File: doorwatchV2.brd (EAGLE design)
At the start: 91.4 x 77.5 mm, 43 parts, among them IC1 LM2576S-5.0, IC2 MAX3232CPE, K1 FINDER-43.61, Q1 IRLZ44Z, T1 BC847, T2 BC847, T3 BC847, T4 BC847, X1 MKDSN1,5/2-5,08, X2 D-SUB9-H2M09RA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

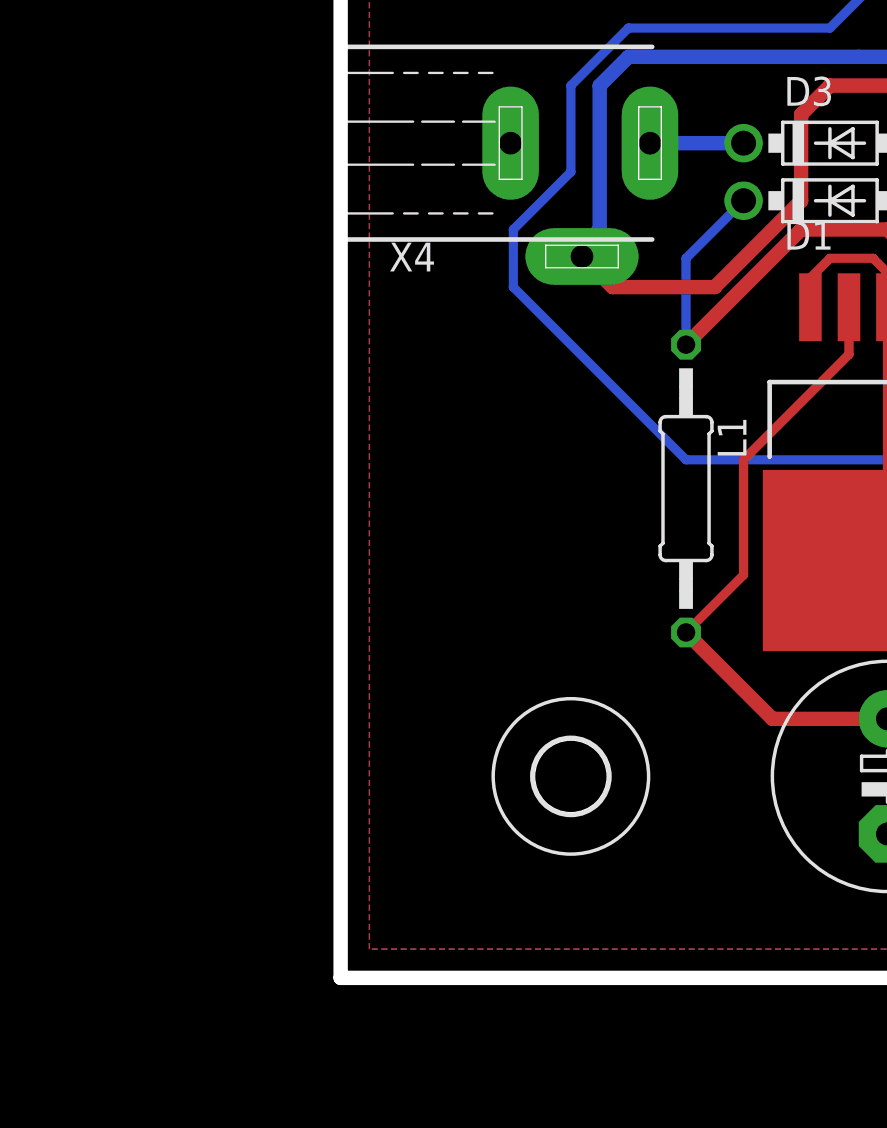
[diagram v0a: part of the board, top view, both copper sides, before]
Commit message: fixed two bugs: 1) wrong polarity of power-jack 2) missing pull-down resistor on output of LTV826 opto-coupler, in front of MOSFET IRLZ44Z
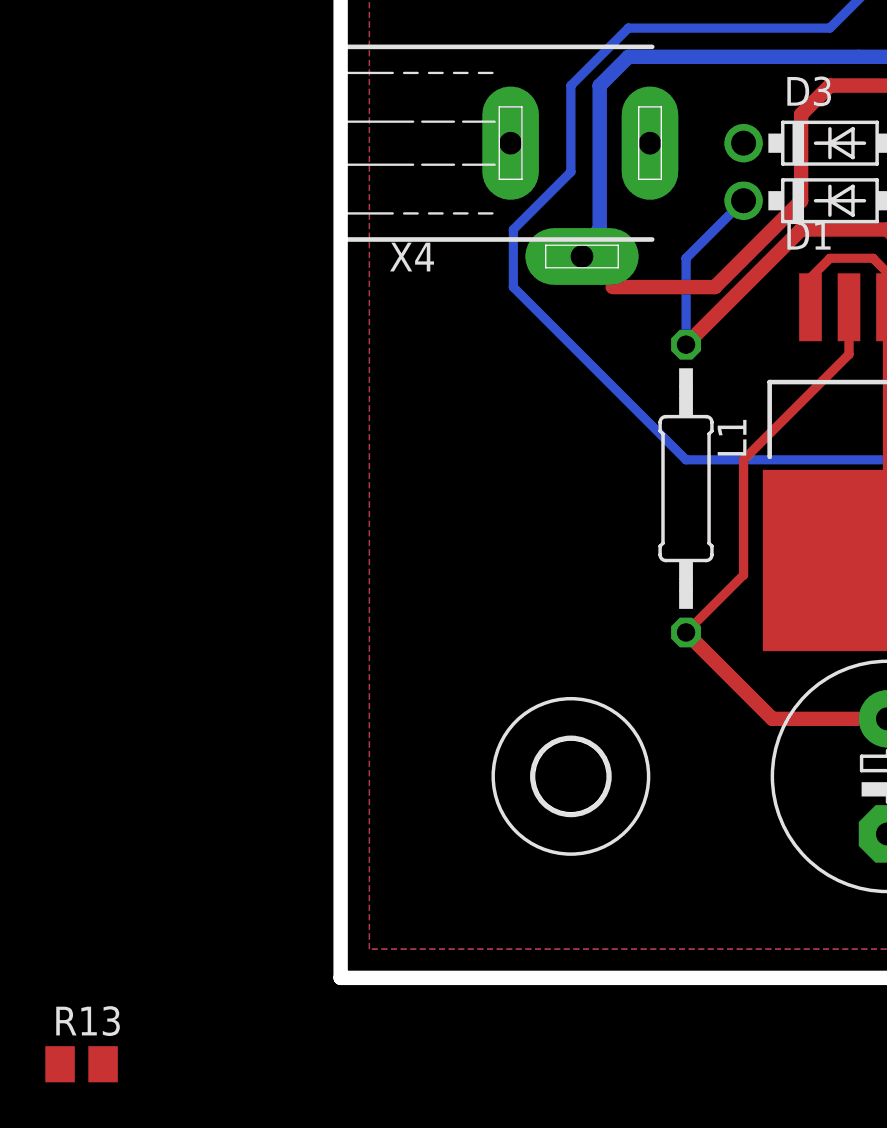
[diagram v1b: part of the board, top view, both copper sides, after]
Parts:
- added R13: 1k, rcl:M0805
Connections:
- net +12V: now also X4.1; no longer X4.3
- net GND: now also R13.1
- net N$15: now also X4.2, X4.3; no longer X4.1
- net N$16: now also R13.2
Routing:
- net N$15: track 4.13 -> 0.00 mm
- net +12V: track 131.0 -> 129.1 mm
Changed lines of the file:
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@@
 <element name="H2" library="holes" package="3,2" value="MOUNT-HOLE3.2" x="55.88" y="93.98"/>
 <element name="H3" library="holes" package="3,2" value="MOUNT-HOLE3.2" x="81.28" y="33.02"/>
+<element name="R13" library="rcl" package="M0805" value="1k" x="-12.7" y="20.32"/>
 </elements>
 <signals>
@@
 <wire x1="20.32" y1="55.88" x2="22.225" y2="55.88" width="0.4064" layer="1"/>
 <wire x1="22.225" y1="55.88" x2="22.86" y2="55.245" width="0.4064" layer="1"/>
+<contactref element="R13" pad="1"/>
+<wire x1="77.47" y1="82.23" x2="82.525" y2="82.5289" width="0" layer="19" extent="16-16"/>
+<wire x1="69.85" y1="55.56" x2="77.47" y2="82.23" width="0" layer="19" extent="16-16"/>
+<wire x1="69.85" y1="46.04" x2="69.85" y2="55.56" width="0" layer="19" extent="16-16"/>
+<wire x1="67.31" y1="31.97" x2="69.85" y2="46.04" width="0" layer="19" extent="1-16"/>
+<wire x1="24.13" y1="58.42" x2="22.225" y2="55.88" width="0" layer="19" extent="1-1"/>
+<wire x1="24.13" y1="60.96" x2="24.13" y2="58.42" width="0" layer="19" extent="1-1"/>
+<wire x1="43.18" y1="63.5" x2="31.75" y2="60.96" width="0" layer="19" extent="1-1"/>
+<wire x1="45.72" y1="58.42" x2="43.18" y2="63.5" width="0" layer="19" extent="1-1"/>
+<wire x1="43.18" y1="53.34" x2="45.72" y2="58.42" width="0" layer="19" extent="1-1"/>
+<wire x1="43.18" y1="71.12" x2="43.18" y2="63.5" width="0" layer="19" extent="1-1"/>
+<wire x1="45.72" y1="78.74" x2="43.18" y2="71.12" width="0" layer="19" extent="1-1"/>
+<wire x1="35.56" y1="78.42" x2="45.72" y2="78.74" width="0" layer="19" extent="16-16"/>
+<wire x1="35.56" y1="84.14" x2="35.56" y2="78.42" width="0" layer="19" extent="16-16"/>
+<wire x1="26.67" y1="75.88" x2="35.56" y2="78.42" width="0" layer="19" extent="16-16"/>
+<wire x1="24.13" y1="76.2" x2="26.67" y2="75.88" width="0" layer="19" extent="16-16"/>
+<wire x1="16.8148" y1="78.2828" x2="24.13" y2="76.2" width="0" layer="19" extent="1-1"/>
+<wire x1="-13.65" y1="20.32" x2="22.86" y2="30.48" width="0" layer="19" extent="1-1"/>
 </signal>
 <signal name="N$3">
@@
 <wire x1="16.51" y1="86.36" x2="16.8148" y2="86.5886" width="0.4064" layer="16"/>
 </signal>
-<signal name="N$15">
-<contactref element="X4" pad="1"/>
-<contactref element="D3" pad="C"/>
-<wire x1="12.38" y1="60.96" x2="16.51" y2="60.96" width="0.635" layer="16"/>
-</signal>
 <signal name="+12V">
 <contactref element="IC1" pad="1"/>
 <contactref element="C1" pad="+"/>
-<contactref element="X4" pad="3"/>
 <contactref element="OK1" pad="6"/>
 <contactref element="Q1" pad="D"/>
@@
 <wire x1="10.16" y1="63.5" x2="10.16" y2="57.15" width="0.635" layer="16"/>
 <wire x1="10.16" y1="57.15" x2="8.89" y2="55.88" width="0.635" layer="16"/>
-<wire x1="10.73" y1="54.61" x2="9.38" y2="55.96" width="0.635" layer="1"/>
 <wire x1="11.43" y1="64.77" x2="21.59" y2="64.77" width="0.635" layer="16"/>
 <wire x1="31.75" y1="64.77" x2="55.88" y2="64.77" width="0.635" layer="16"/>
 <wire x1="21.59" y1="64.77" x2="31.75" y2="64.77" width="0.635" layer="16"/>
-<wire x1="9.38" y1="55.96" x2="8.89" y2="55.88" width="0" layer="19" extent="16-16"/>
+<contactref element="X4" pad="1"/>
+<wire x1="10.16" y1="63.5" x2="12.38" y2="60.96" width="0" layer="19" extent="16-16"/>
+<wire x1="20.32" y1="63.5" x2="21.59" y2="64.77" width="0" layer="19" extent="1-16"/>
 </signal>
 <signal name="N$10">
@@
 <contactref element="R3" pad="1"/>
 <wire x1="74.93" y1="48.26" x2="79.06" y2="48.26" width="0.4064" layer="16"/>
+<contactref element="R13" pad="2"/>
+<wire x1="-11.75" y1="20.32" x2="74.93" y2="48.26" width="0" layer="19" extent="1-1"/>
 </signal>
 <signal name="N$17">
@@
 </polygon>
 </signal>
+<signal name="N$15">
+<contactref element="X4" pad="3"/>
+<contactref element="X4" pad="2"/>
+<contactref element="D3" pad="C"/>
+<wire x1="9.38" y1="55.96" x2="16.51" y2="60.96" width="0" layer="19" extent="1-1"/>
+<wire x1="6.23" y1="60.96" x2="9.38" y2="55.96" width="0" layer="19" extent="1-1"/>
+</signal>
 </signals>

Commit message: updated changes in layout
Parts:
- moved R13 89.2 mm to (72.4, 47.0), flipped to the bottom, turned to 90 degrees
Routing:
- net +12V: track 129.1 -> 100.1 mm
- net N$15: track 0.00 -> 15.5 mm
- net +3V3: track 77.5 -> 84.4 mm
- net N$16: track 4.13 -> 6.99 mm
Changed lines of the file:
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@@
 <element name="H2" library="holes" package="3,2" value="MOUNT-HOLE3.2" x="55.88" y="93.98"/>
 <element name="H3" library="holes" package="3,2" value="MOUNT-HOLE3.2" x="81.28" y="33.02"/>
-<element name="R13" library="rcl" package="M0805" value="1k" x="-12.7" y="20.32"/>
+<element name="R13" library="rcl" package="M0805" value="1k" x="72.39" y="46.99" rot="MR90"/>
 </elements>
 <signals>
@@
 <wire x1="22.225" y1="55.88" x2="22.86" y2="55.245" width="0.4064" layer="1"/>
 <contactref element="R13" pad="1"/>
-<wire x1="77.47" y1="82.23" x2="82.525" y2="82.5289" width="0" layer="19" extent="16-16"/>
-<wire x1="69.85" y1="55.56" x2="77.47" y2="82.23" width="0" layer="19" extent="16-16"/>
-<wire x1="69.85" y1="46.04" x2="69.85" y2="55.56" width="0" layer="19" extent="16-16"/>
-<wire x1="67.31" y1="31.97" x2="69.85" y2="46.04" width="0" layer="19" extent="1-16"/>
-<wire x1="24.13" y1="58.42" x2="22.225" y2="55.88" width="0" layer="19" extent="1-1"/>
-<wire x1="24.13" y1="60.96" x2="24.13" y2="58.42" width="0" layer="19" extent="1-1"/>
-<wire x1="43.18" y1="63.5" x2="31.75" y2="60.96" width="0" layer="19" extent="1-1"/>
-<wire x1="45.72" y1="58.42" x2="43.18" y2="63.5" width="0" layer="19" extent="1-1"/>
-<wire x1="43.18" y1="53.34" x2="45.72" y2="58.42" width="0" layer="19" extent="1-1"/>
-<wire x1="43.18" y1="71.12" x2="43.18" y2="63.5" width="0" layer="19" extent="1-1"/>
-<wire x1="45.72" y1="78.74" x2="43.18" y2="71.12" width="0" layer="19" extent="1-1"/>
-<wire x1="35.56" y1="78.42" x2="45.72" y2="78.74" width="0" layer="19" extent="16-16"/>
-<wire x1="35.56" y1="84.14" x2="35.56" y2="78.42" width="0" layer="19" extent="16-16"/>
-<wire x1="26.67" y1="75.88" x2="35.56" y2="78.42" width="0" layer="19" extent="16-16"/>
-<wire x1="24.13" y1="76.2" x2="26.67" y2="75.88" width="0" layer="19" extent="16-16"/>
-<wire x1="16.8148" y1="78.2828" x2="24.13" y2="76.2" width="0" layer="19" extent="1-1"/>
-<wire x1="-13.65" y1="20.32" x2="22.86" y2="30.48" width="0" layer="19" extent="1-1"/>
 </signal>
 <signal name="N$3">
@@
 <wire x1="24.56" y1="55.45" x2="22.86" y2="57.15" width="0.635" layer="1"/>
 <wire x1="22.86" y1="57.15" x2="19.05" y2="57.15" width="0.635" layer="1"/>
-<wire x1="16.51" y1="58.42" x2="13.97" y2="55.88" width="0.4064" layer="16"/>
 <wire x1="13.97" y1="55.88" x2="13.97" y2="52.07" width="0.4064" layer="16"/>
 <wire x1="19.05" y1="57.15" x2="13.97" y2="52.07" width="0.635" layer="1"/>
+<wire x1="16.51" y1="58.42" x2="13.97" y2="55.88" width="0.4064" layer="16"/>
 </signal>
 <signal name="+5V">
@@
 <wire x1="44.45" y1="46.99" x2="45.72" y2="48.26" width="0.4064" layer="16"/>
 <wire x1="13.97" y1="46.99" x2="44.45" y2="46.99" width="0.4064" layer="16"/>
-<wire x1="13.97" y1="46.99" x2="6.35" y2="54.61" width="0.4064" layer="16"/>
-<wire x1="6.35" y1="54.61" x2="6.35" y2="57.15" width="0.4064" layer="16"/>
-<wire x1="6.35" y1="57.15" x2="8.89" y2="59.69" width="0.4064" layer="16"/>
-<wire x1="8.89" y1="59.69" x2="8.89" y2="63.5" width="0.4064" layer="16"/>
-<wire x1="8.89" y1="63.5" x2="11.43" y2="66.04" width="0.4064" layer="16"/>
-<wire x1="11.43" y1="66.04" x2="20.32" y2="66.04" width="0.4064" layer="16"/>
+<wire x1="13.97" y1="46.99" x2="2.54" y2="58.42" width="0.4064" layer="16"/>
+<wire x1="5.08" y1="66.04" x2="20.32" y2="66.04" width="0.4064" layer="16"/>
 <wire x1="20.32" y1="66.04" x2="24.13" y2="69.85" width="0.4064" layer="16"/>
 <wire x1="24.13" y1="69.85" x2="24.13" y2="73.66" width="0.4064" layer="16"/>
+<wire x1="2.54" y1="58.42" x2="2.54" y2="63.5" width="0.4064" layer="16"/>
+<wire x1="2.54" y1="63.5" x2="5.08" y2="66.04" width="0.4064" layer="16"/>
 </signal>
 <signal name="GPIO2">
@@
 <contactref element="OK1" pad="8"/>
 <contactref element="T3" pad="3"/>
-<wire x1="15.24" y1="54.61" x2="19.05" y2="58.42" width="0.635" layer="1"/>
-<wire x1="10.73" y1="54.61" x2="15.24" y2="54.61" width="0.635" layer="1"/>
-<wire x1="26.67" y1="62.23" x2="26.67" y2="54.61" width="0.635" layer="1"/>
-<wire x1="25.4" y1="63.5" x2="26.67" y2="62.23" width="0.635" layer="1"/>
-<wire x1="26.67" y1="54.61" x2="26.26" y2="53.72" width="0.4064" layer="1"/>
 <wire x1="80.01" y1="58.42" x2="80.01" y2="58.25" width="0.4064" layer="16"/>
 <wire x1="73.66" y1="52.07" x2="74.93" y2="50.8" width="0.4064" layer="1"/>
@@
 <wire x1="73.66" y1="59.69" x2="74.93" y2="58.42" width="0.4064" layer="16"/>
 <wire x1="74.93" y1="58.42" x2="74.93" y2="55.88" width="0.4064" layer="16"/>
-<wire x1="10.16" y1="63.5" x2="11.43" y2="64.77" width="0.635" layer="16"/>
-<wire x1="19.05" y1="58.42" x2="19.05" y2="62.23" width="0.635" layer="1"/>
-<wire x1="19.05" y1="62.23" x2="20.32" y2="63.5" width="0.635" layer="1"/>
-<wire x1="20.32" y1="63.5" x2="25.4" y2="63.5" width="0.635" layer="1"/>
 <wire x1="80.01" y1="58.42" x2="74.93" y2="58.42" width="0.4064" layer="16"/>
-<wire x1="31.75" y1="58.42" x2="30.48" y2="58.42" width="0.635" layer="1"/>
-<wire x1="30.48" y1="58.42" x2="26.67" y2="54.61" width="0.635" layer="1"/>
-<wire x1="10.16" y1="63.5" x2="10.16" y2="57.15" width="0.635" layer="16"/>
-<wire x1="10.16" y1="57.15" x2="8.89" y2="55.88" width="0.635" layer="16"/>
-<wire x1="11.43" y1="64.77" x2="21.59" y2="64.77" width="0.635" layer="16"/>
-<wire x1="31.75" y1="64.77" x2="55.88" y2="64.77" width="0.635" layer="16"/>
-<wire x1="21.59" y1="64.77" x2="31.75" y2="64.77" width="0.635" layer="16"/>
 <contactref element="X4" pad="1"/>
-<wire x1="10.16" y1="63.5" x2="12.38" y2="60.96" width="0" layer="19" extent="16-16"/>
-<wire x1="20.32" y1="63.5" x2="21.59" y2="64.77" width="0" layer="19" extent="1-16"/>
+<wire x1="55.88" y1="64.77" x2="34.29" y2="64.77" width="0.6096" layer="16"/>
+<wire x1="15.24" y1="64.77" x2="12.38" y2="61.91" width="0.6096" layer="16"/>
+<wire x1="12.38" y1="61.91" x2="12.38" y2="60.96" width="0.6096" layer="16"/>
+<wire x1="26.26" y1="53.72" x2="30.96" y2="58.42" width="0.6096" layer="1"/>
+<wire x1="30.96" y1="58.42" x2="31.75" y2="58.42" width="0.6096" layer="1"/>
+<wire x1="15.24" y1="64.77" x2="34.29" y2="64.77" width="0.6096" layer="16"/>
+<wire x1="34.29" y1="64.77" x2="35.56" y2="63.5" width="0.6096" layer="16"/>
+<wire x1="35.56" y1="63.5" x2="35.56" y2="59.69" width="0.6096" layer="16"/>
+<wire x1="35.56" y1="59.69" x2="34.29" y2="58.42" width="0.6096" layer="16"/>
+<wire x1="34.29" y1="58.42" x2="31.75" y2="58.42" width="0.6096" layer="16"/>
 </signal>
 <signal name="N$10">
@@
 <wire x1="74.93" y1="48.26" x2="79.06" y2="48.26" width="0.4064" layer="16"/>
 <contactref element="R13" pad="2"/>
-<wire x1="-11.75" y1="20.32" x2="74.93" y2="48.26" width="0" layer="19" extent="1-1"/>
+<wire x1="74.93" y1="48.26" x2="72.39" y2="48.26" width="0.4064" layer="16"/>
+<wire x1="72.39" y1="48.26" x2="72.39" y2="47.94" width="0.4064" layer="16"/>
 </signal>
 <signal name="N$17">
@@
 <contactref element="X4" pad="2"/>
 <contactref element="D3" pad="C"/>
-<wire x1="9.38" y1="55.96" x2="16.51" y2="60.96" width="0" layer="19" extent="1-1"/>
-<wire x1="6.23" y1="60.96" x2="9.38" y2="55.96" width="0" layer="19" extent="1-1"/>
+<wire x1="16.51" y1="60.96" x2="11.51" y2="55.96" width="0.6096" layer="16"/>
+<wire x1="11.51" y1="55.96" x2="9.38" y2="55.96" width="0.6096" layer="16"/>
+<wire x1="9.38" y1="55.96" x2="6.23" y2="59.11" width="0.6096" layer="16"/>
+<wire x1="6.23" y1="59.11" x2="6.23" y2="60.96" width="0.6096" layer="16"/>
 </signal>
 </signals>
